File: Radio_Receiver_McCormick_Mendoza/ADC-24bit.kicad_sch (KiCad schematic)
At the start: 24 parts, among them J21 SDR Out, J22 Q_OUT, J7 I_OUT, U10 OPA1612AxD, U12 PCM1808PWR

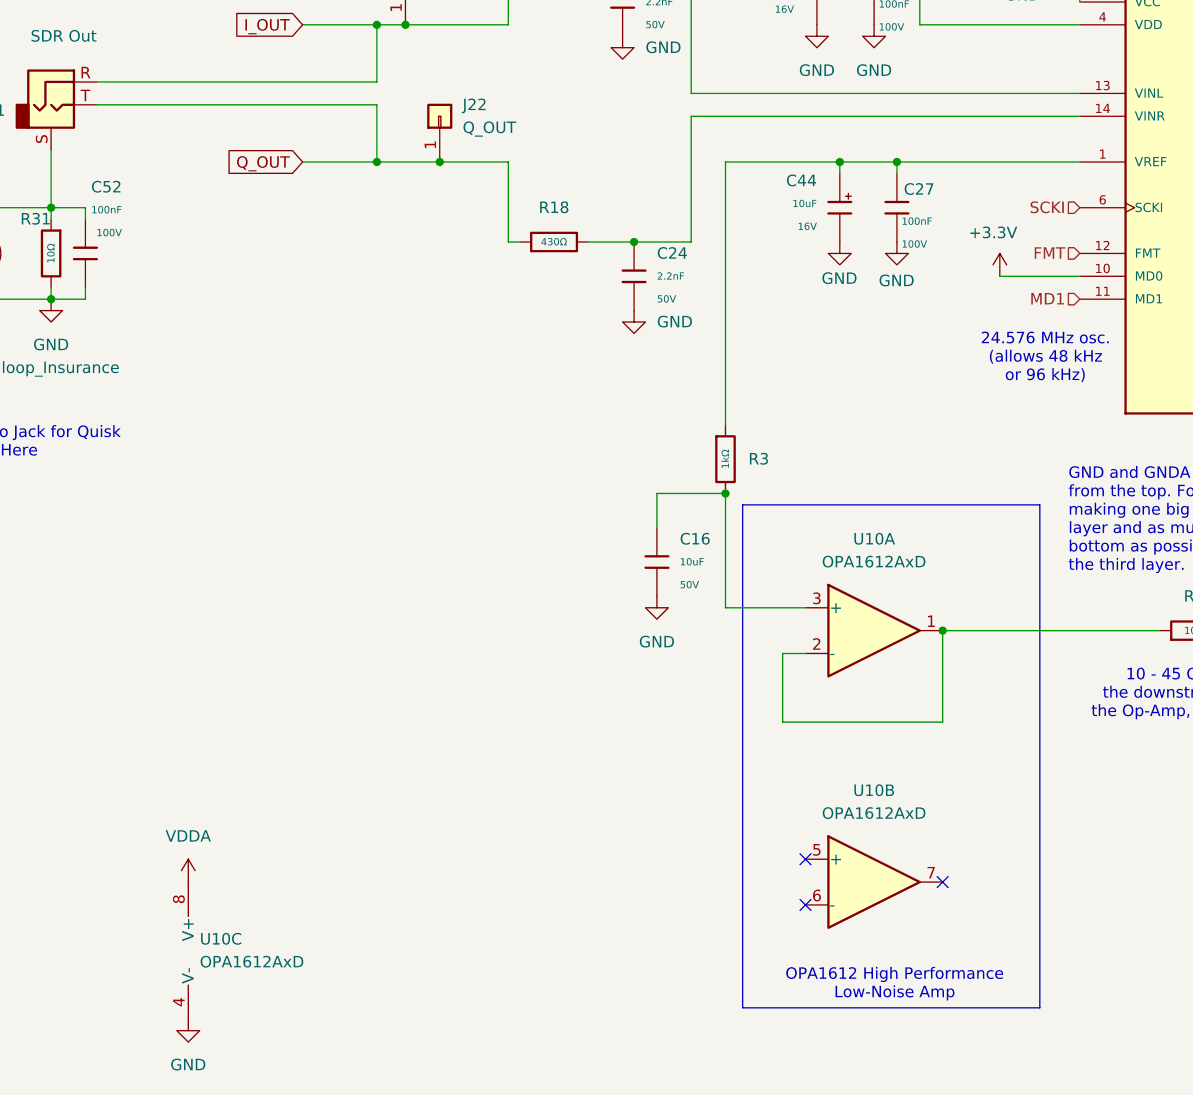
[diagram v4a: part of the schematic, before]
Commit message: Isolated filter switching MUX from digital control
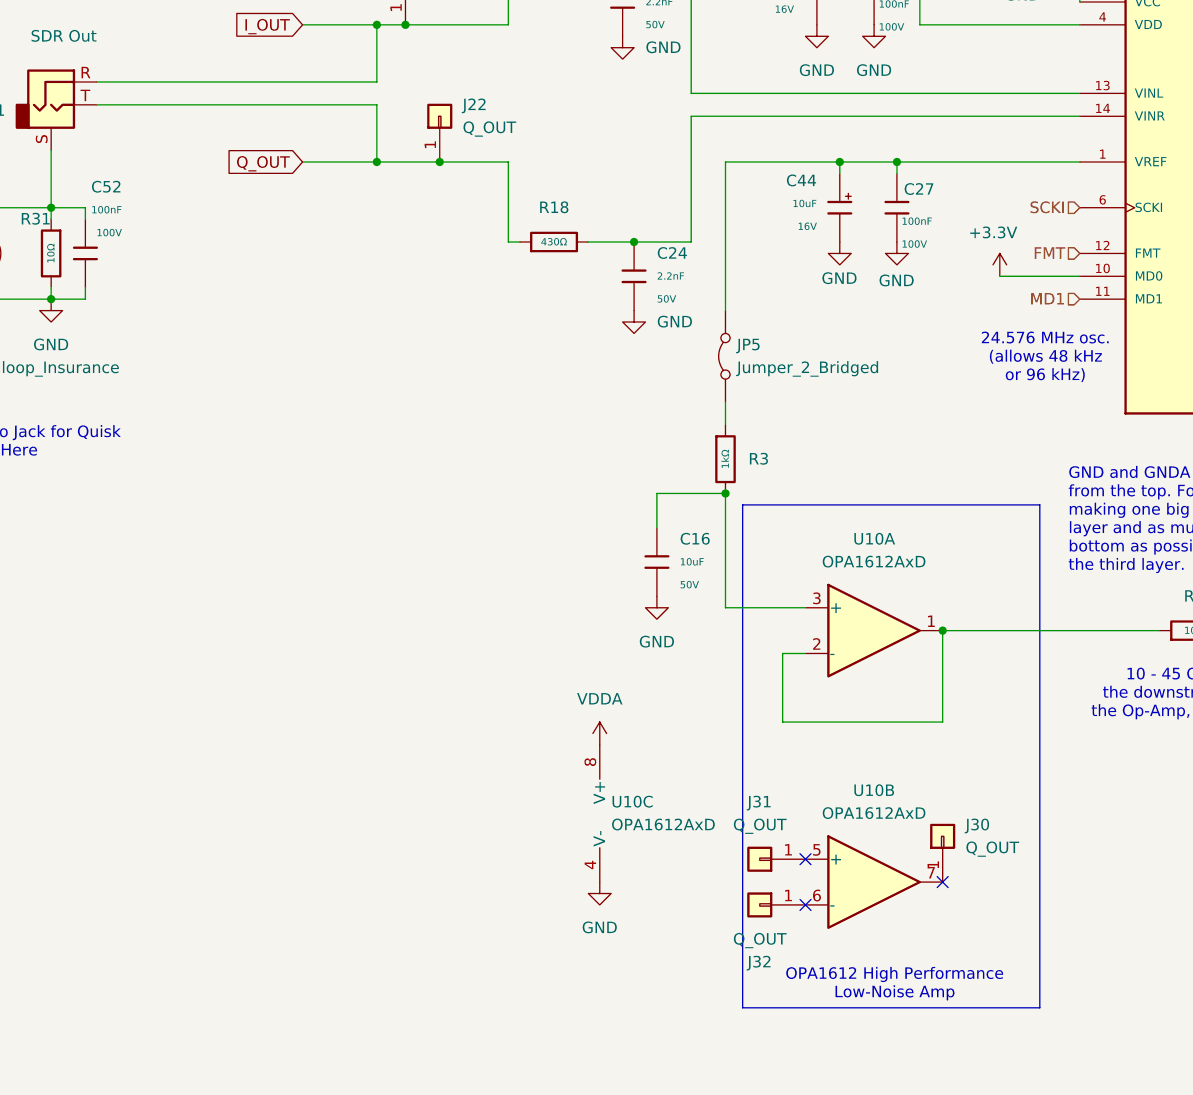
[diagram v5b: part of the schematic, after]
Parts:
- added J30, J31, J32: Q_OUT, Connector_PinHeader_2.54mm:PinHeader_1x01_P2.54mm_Vertical, symbol Connector_Generic:Conn_01x01
- added JP5: Jumper_2_Bridged, symbol Jumper:Jumper_2_Bridged
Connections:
- net at C27.2, C44.1, U12.1 (VREF): now also JP5.2 (B); no longer R3.1
- net at U10.5 (+): now also J31.1 (Pin_1)
- net at U10.6 (-): now also J32.1 (Pin_1)
- net at U10.7: now also J30.1 (Pin_1)
- new net: JP5.1 (A), R3.1
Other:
- moved on the sheet: U10C

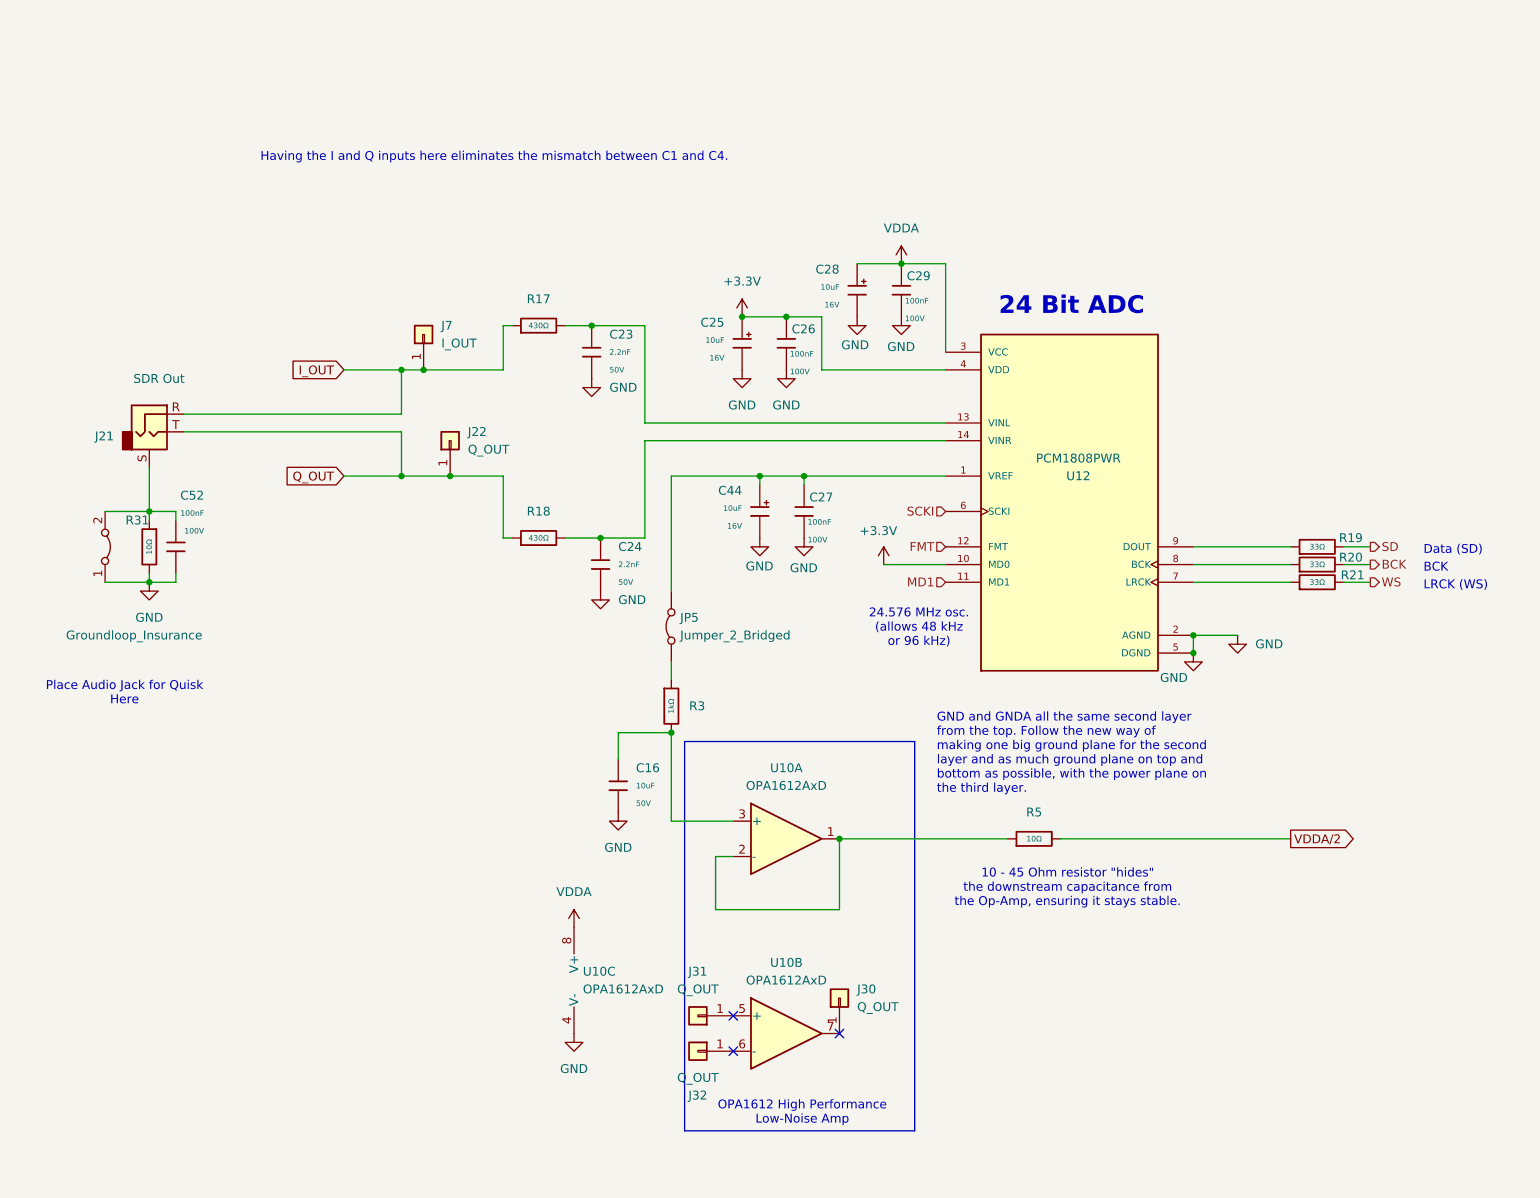
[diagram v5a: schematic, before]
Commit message: Added DAC and shaft angle encoder
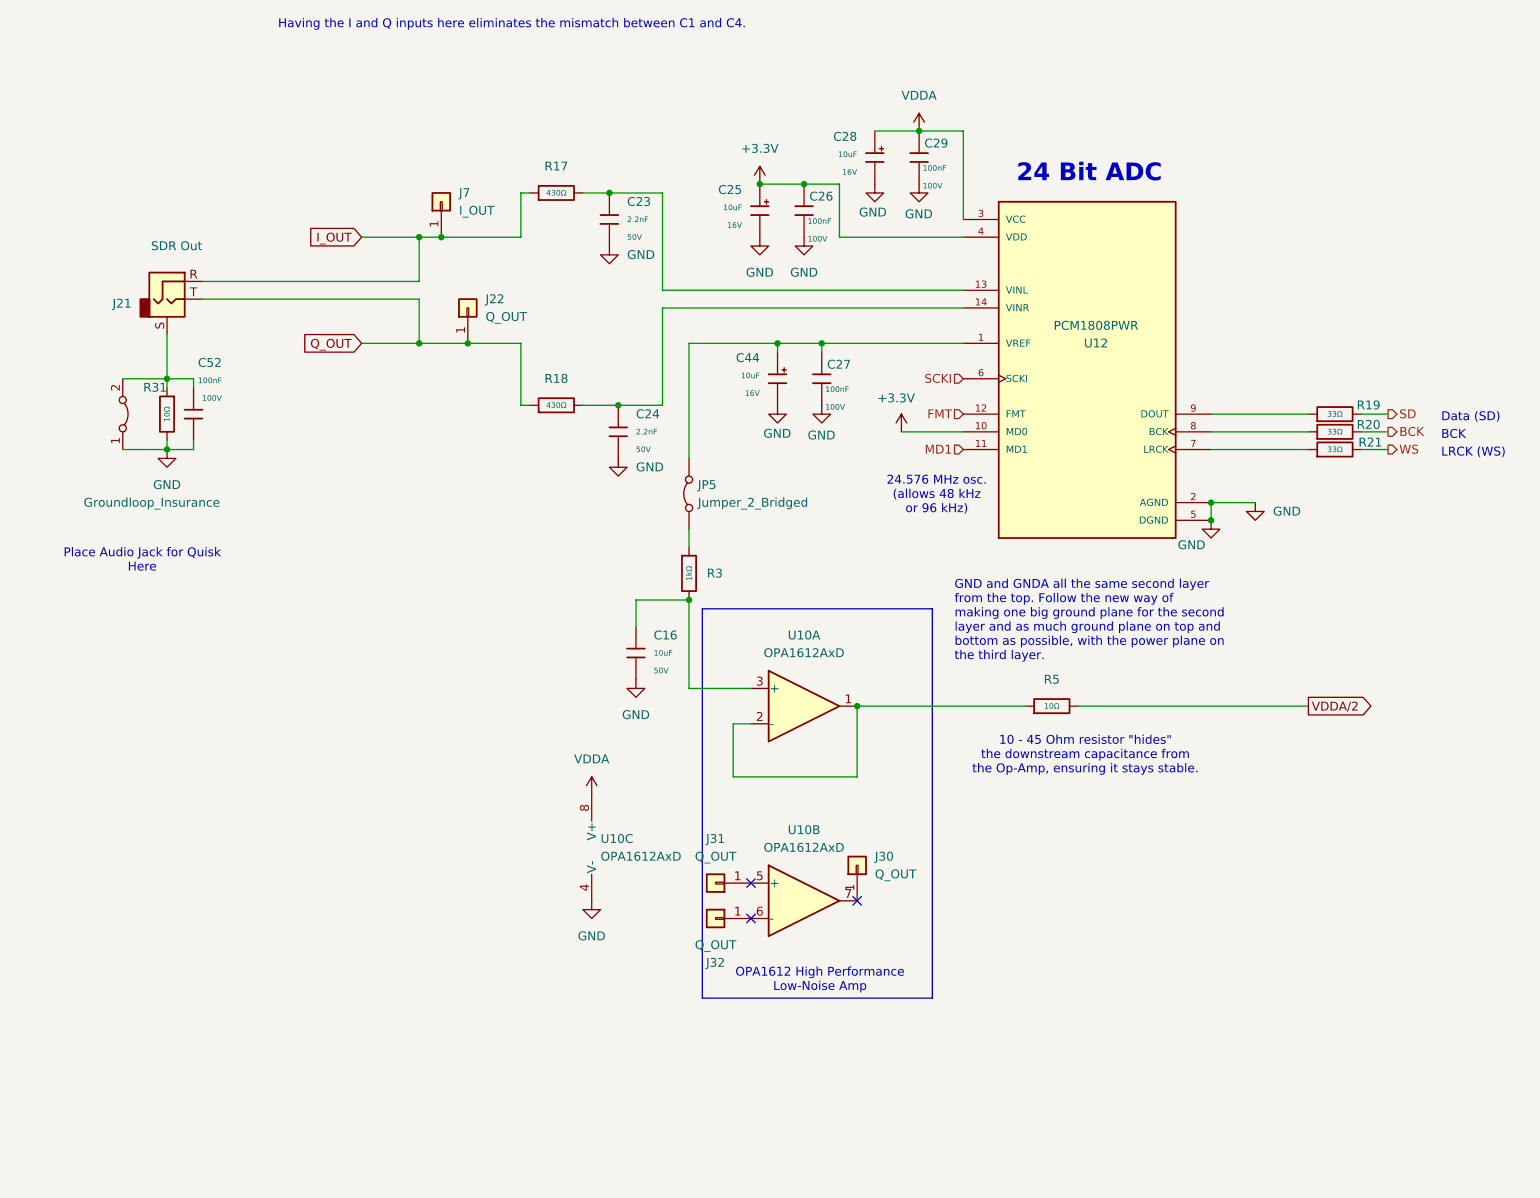
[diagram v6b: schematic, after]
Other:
- moved on the sheet: C16, C23, C24, C25, C26, C27, C28, C29, C44, C52, J21, J22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

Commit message: Added digital power regulator
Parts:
- C16: Manufacturer Murata Electronics -> (none)
- C23, C24, C26, C27, C29, C52: Manufacturer Samsung Electro-Mechanics -> (none)
- C25, C28, C44: Manufacturer AVX -> (none)
- R17, R18, R19, R20, R21, R3, R31, R5: Manufacturer UNI-ROYAL(Uniroyal Elec) -> (none)
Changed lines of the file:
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@@
 			)
 		)
-		(property "Manufacturer" "UNI-ROYAL(Uniroyal Elec)"
-			(at 52.07 81.28 0)
-			(hide yes)
-			(show_name no)
-			(do_not_autoplace no)
-			(effects
-				(font
-					(size 1.27 1.27)
-				)
-			)
-		)
 		(property "Part" "0603WAF100JT5E"
 			(at 52.07 81.28 0)
@@
 			)
 		)
-		(property "Manufacturer" "Samsung Electro-Mechanics"
-			(at 115.57 53.34 0)
-			(hide yes)
-			(show_name no)
-			(do_not_autoplace no)
-			(effects
-				(font
-					(size 1.27 1.27)
-				)
-			)
-		)
 		(property "Part" "CL21C222JBFNNNE"
 			(at 115.57 53.34 0)
@@
 			)
 		)
-		(property "Manufacturer" "Samsung Electro-Mechanics"
-			(at 55.88 81.28 0)
-			(hide yes)
-			(show_name no)
-			(do_not_autoplace no)
-			(effects
-				(font
-					(size 1.27 1.27)
-				)
-			)
-		)
 		(property "Part" "CL21B104KCFNNNE"
 			(at 55.88 81.28 0)
@@
 			)
 		)
-		(property "Manufacturer" "UNI-ROYAL(Uniroyal Elec)"
-			(at 107.95 80.01 0)
-			(hide yes)
-			(show_name no)
-			(do_not_autoplace no)
-			(effects
-				(font
-					(size 1.27 1.27)
-				)
-			)
-		)
 		(property "Part" "0603WAF4300T5E"
 			(at 107.95 80.01 0)
@@
 			)
 		)
-		(property "Manufacturer" "AVX"
-			(at 137.16 52.07 0)
-			(hide yes)
-			(show_name no)
-			(do_not_autoplace no)
-			(effects
-				(font
-					(size 1.27 1.27)
-				)
-			)
-		)
 		(property "Part" "TAJA106K016RNJ"
 			(at 137.16 52.07 0)
@@
 			)
 		)
-		(property "Manufacturer" "Murata Electronics"
-			(at 119.38 115.57 0)
-			(hide yes)
-			(show_name no)
-			(do_not_autoplace no)
-			(effects
-				(font
-					(size 1.27 1.27)
-				)
-			)
-		)
 		(property "Part" "GRM21BR61H106KE43L"
 			(at 119.38 115.57 0)
@@
 			)
 		)
-		(property "Manufacturer" "UNI-ROYAL(Uniroyal Elec)"
-			(at 127 104.14 0)
-			(hide yes)
-			(show_name no)
-			(do_not_autoplace no)
-			(effects
-				(font
-					(size 1.27 1.27)
-				)
-			)
-		)
 		(property "Part" "0402WGF1001TCE"
 			(at 127 104.14 0)
@@
 			)
 		)
-		(property "Manufacturer" "Samsung Electro-Mechanics"
-			(at 116.84 83.82 0)
-			(hide yes)
-			(show_name no)
-			(do_not_autoplace no)
-			(effects
-				(font
-					(size 1.27 1.27)
-				)
-			)
-		)
 		(property "Part" "CL21C222JBFNNNE"
 			(at 116.84 83.82 0)
@@
 			)
 		)
-		(property "Manufacturer" "UNI-ROYAL(Uniroyal Elec)"
-			(at 107.95 49.53 0)
-			(hide yes)
-			(show_name no)
-			(do_not_autoplace no)
-			(effects
-				(font
-					(size 1.27 1.27)
-				)
-			)
-		)
 		(property "Part" "0603WAF4300T5E"
 			(at 107.95 49.53 0)
@@
 			)
 		)
-		(property "Manufacturer" "UNI-ROYAL(Uniroyal Elec)"
-			(at 219.71 86.36 0)
-			(hide yes)
-			(show_name no)
-			(do_not_autoplace no)
-			(effects
-				(font
-					(size 1.27 1.27)
-				)
-			)
-		)
 		(property "Part" "0805W8F330JT5E"
 			(at 219.71 86.36 0)
@@
 			)
 		)
-		(property "Manufacturer" "UNI-ROYAL(Uniroyal Elec)"
-			(at 219.71 81.28 0)
-			(hide yes)
-			(show_name no)
-			(do_not_autoplace no)
-			(effects
-				(font
-					(size 1.27 1.27)
-				)
-			)
-		)
 		(property "Part" "0805W8F330JT5E"
 			(at 219.71 81.28 0)
@@
 			)
 		)
-		(property "Manufacturer" "Samsung Electro-Mechanics"
-			(at 143.51 52.07 0)
-			(hide yes)
-			(show_name no)
-			(do_not_autoplace no)
-			(effects
-				(font
-					(size 1.27 1.27)
-				)
-			)
-		)
 		(property "Part" "CL21B104KCFNNNE"
 			(at 143.51 52.07 0)
@@
 			)
 		)
-		(property "Manufacturer" "AVX"
-			(at 153.67 44.45 0)
-			(hide yes)
-			(show_name no)
-			(do_not_autoplace no)
-			(effects
-				(font
-					(size 1.27 1.27)
-				)
-			)
-		)
 		(property "Part" "TAJA106K016RNJ"
 			(at 153.67 44.45 0)
@@
 			)
 		)
-		(property "Manufacturer" "Samsung Electro-Mechanics"
-			(at 146.05 76.2 0)
-			(hide yes)
-			(show_name no)
-			(do_not_autoplace no)
-			(effects
-				(font
-					(size 1.27 1.27)
-				)
-			)
-		)
 		(property "Part" "CL21B104KCFNNNE"
 			(at 146.05 76.2 0)
@@
 			)
 		)
-		(property "Manufacturer" "UNI-ROYAL(Uniroyal Elec)"
-			(at 219.71 83.82 0)
-			(hide yes)
-			(show_name no)
-			(do_not_autoplace no)
-			(effects
-				(font
-					(size 1.27 1.27)
-				)
-			)
-		)
 		(property "Part" "0805W8F330JT5E"
 			(at 219.71 83.82 0)
@@
 			)
 		)
-		(property "Manufacturer" "UNI-ROYAL(Uniroyal Elec)"
-			(at 179.07 123.19 0)
-			(hide yes)
-			(show_name no)
-			(do_not_autoplace no)
-			(effects
-				(font
-					(size 1.27 1.27)
-				)
-			)
-		)
 		(property "Part" "0805W8F100JT5E"
 			(at 179.07 123.19 0)
@@
 			)
 		)
-		(property "Manufacturer" "Samsung Electro-Mechanics"
-			(at 160.02 44.45 0)
-			(hide yes)
-			(show_name no)
-			(do_not_autoplace no)
-			(effects
-				(font
-					(size 1.27 1.27)
-				)
-			)
-		)
 		(property "Part" "CL21B104KCFNNNE"
 			(at 160.02 44.45 0)
@@
 			(at 139.7 76.2 0)
 			(hide yes)
-			(show_name no)
-			(do_not_autoplace no)
-			(effects
-				(font
-					(size 1.27 1.27)
-				)
-			)
-		)
-		(property "Manufacturer" "AVX"
-			(at 139.7 76.2 0)
-			(hide yes)
